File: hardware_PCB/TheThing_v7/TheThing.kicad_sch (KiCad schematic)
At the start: 69 parts, among them J1 Conn_I2C, J10 Conn_01x03, J11 Conn_01x03, J12 Conn_01x03, J13 Conn_01x03, J14 Conn_01x03, J17 Conn_01x10, J18 Conn_01x15, J19 Conn_01x15, J2 Conn_I2C, J20 D2, J21 D3, J22 D4, J23 D5, J24 D6, J25 D7, J26 D8, J27 D9, J28 D10, J29 D11, J3 Conn_01x03, J30 D12, J31 D13, J32 RST1, J33 RST1, J34 D0, J35 D1, J36 A7, J37 A6, J38 A5, J39 A4, J4 Conn_01x03, J40 A3, J41 A2, J42 A1, J43 A0, J44 AREF, J45 VIN, J46 5V, J47 3V3, J48 GND1, J49 GND2, J5 Conn_01x03, J6 Conn_01x03, J7 Conn_01x03, J8 Conn_01x03, J9 Conn_01x03, SW1 ON, U1 Arduino_Nano

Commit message: v7 prototype files for PCB and enclosure
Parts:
- R13, R14, R15, R16, R17: value 22k -> 20k
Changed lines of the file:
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@@
 			)
 		)
-		(property "Value" "22k"
+		(property "Value" "20k"
 			(at 157.48 139.7 90)
 			(effects
@@
 			)
 		)
-		(property "Value" "22k"
+		(property "Value" "20k"
 			(at 167.64 139.7 90)
 			(effects
@@
 			)
 		)
-		(property "Value" "22k"
+		(property "Value" "20k"
 			(at 162.56 139.7 90)
 			(effects
@@
 			)
 		)
-		(property "Value" "22k"
+		(property "Value" "20k"
 			(at 147.32 139.7 90)
 			(effects
@@
 			)
 		)
-		(property "Value" "22k"
+		(property "Value" "20k"
 			(at 152.4 139.7 90)
 			(effects

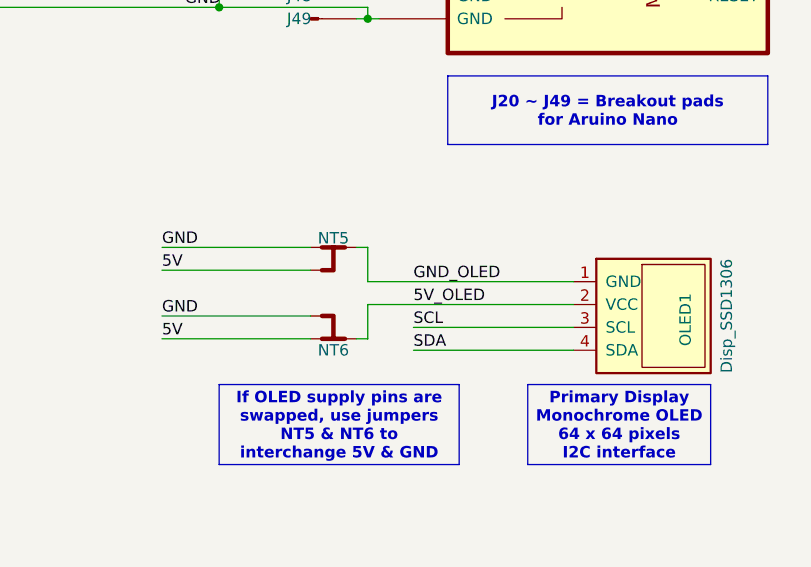
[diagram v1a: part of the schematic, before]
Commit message: fixed default OLED jumper connections
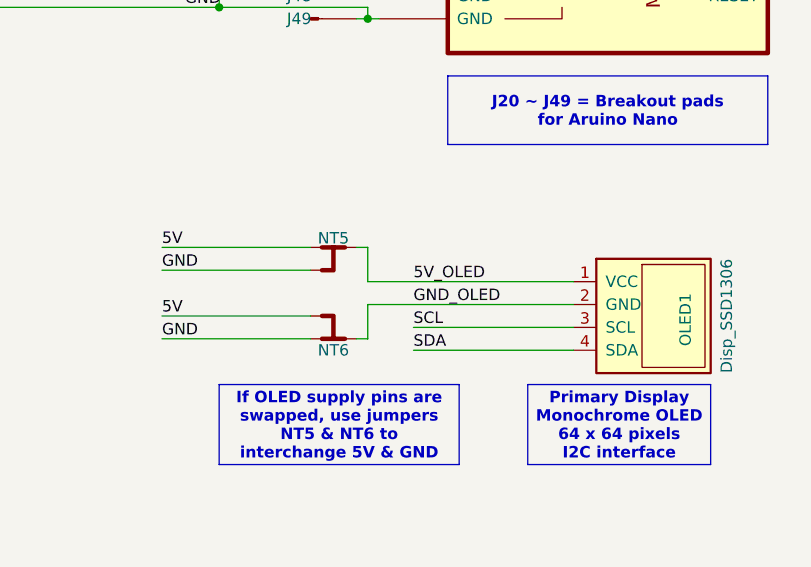
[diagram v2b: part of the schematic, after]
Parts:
- OLED1: symbol TheThing:Disp_SSD1306 -> TheThing:Disp_SSD1306_v2
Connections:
- net 5V: now also NT5.1, NT6.3; no longer NT5.3, NT6.1
- net 5V_OLED: now also NT5.2, OLED1.1 (VCC); no longer NT6.2, OLED1.2 (VCC)
- net GND: now also NT5.3, NT6.1; no longer NT5.1, NT6.3
- net GND_OLED: now also NT6.2, OLED1.2 (GND); no longer NT5.2, OLED1.1 (GND)
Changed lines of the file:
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@@
 	(title_block
 		(title "TheThing")
-		(date "2025-05-09")
+		(date "2025-05-16")
 		(rev "v7")
 		(company "Maker's Asylum")
@@
 	)
 	(label "5V_OLED"
-		(at 78.74 104.14 0)
+		(at 78.74 101.6 0)
 		(effects
 			(font
@@
 	)
 	(label "5V"
-		(at 50.8 107.95 0)
+		(at 50.8 105.41 0)
 		(effects
 			(font
@@
 	)
 	(label "GND_OLED"
-		(at 78.74 101.6 0)
+		(at 78.74 104.14 0)
 		(effects
 			(font
@@
 	)
 	(label "GND"
-		(at 50.8 97.79 0)
+		(at 50.8 100.33 0)
 		(effects
 			(font
@@
 	)
 	(label "5V"
-		(at 50.8 100.33 0)
+		(at 50.8 97.79 0)
 		(effects
 			(font
@@
 	)
 	(label "GND"
-		(at 50.8 105.41 0)
+		(at 50.8 107.95 0)
 		(effects
 			(font
@@
 	)
 	(symbol
-		(lib_id "TheThing:Disp_SSD1306")
+		(lib_id "TheThing:Disp_SSD1306_v2")
 		(at 105.41 105.41 90)
 		(mirror x)
